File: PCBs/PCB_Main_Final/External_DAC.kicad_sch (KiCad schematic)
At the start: 15 parts, among them U9 PCM5102A

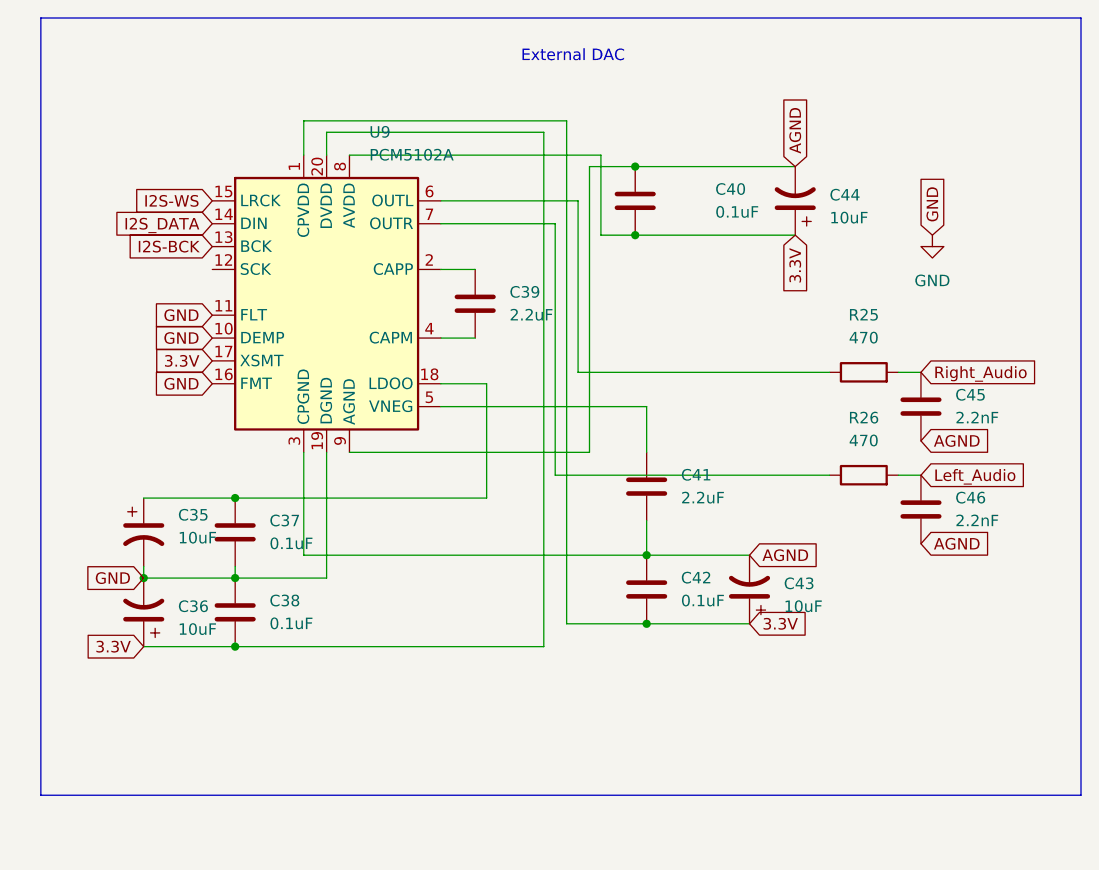
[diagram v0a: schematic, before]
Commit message: fixed vias and expanded boost converter
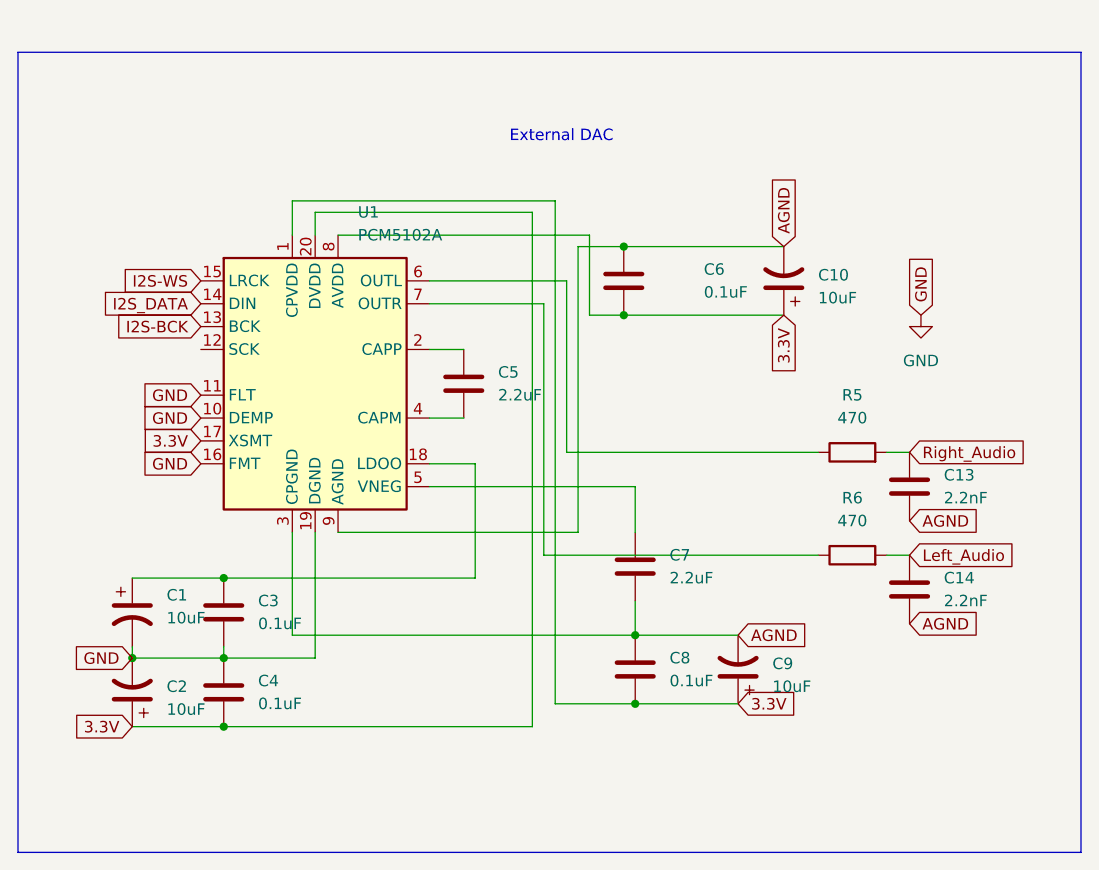
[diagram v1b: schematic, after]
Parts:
- removed C35, C36, C43, C44: 10uF, Artisyn_Components:EX_DAC_ELEC_CAPS_10uF, symbol Device:C_Polarized_US
- removed C37, C38, C40, C42: 0.1uF, Capacitor_SMD:C_0805_2012Metric, symbol Device:C
- removed C39, C41: 2.2uF, Capacitor_SMD:C_0805_2012Metric, symbol Device:C
- removed C45, C46: 2.2nF, Capacitor_SMD:C_0805_2012Metric, symbol Device:C
- removed R25, R26: 470, Resistor_SMD:R_0805_2012Metric, symbol Device:R
- removed U9: PCM5102A, Package_SO:TSSOP-20_4.4x6.5mm_P0.65mm, symbol Audio:PCM5102A
- added C1, C10, C2, C9: 10uF, Artisyn_Components:EX_DAC_ELEC_CAPS_10uF, symbol Device:C_Polarized_US
- added C13, C14: 2.2nF, Capacitor_SMD:C_0805_2012Metric, symbol Device:C
- added C3, C4, C6, C8: 0.1uF, Capacitor_SMD:C_0805_2012Metric, symbol Device:C
- added C5, C7: 2.2uF, Capacitor_SMD:C_0805_2012Metric, symbol Device:C
- added R5, R6: 470, Resistor_SMD:R_0805_2012Metric, symbol Device:R
- added U1: PCM5102A, Package_SO:TSSOP-20_4.4x6.5mm_P0.65mm, symbol Audio:PCM5102A
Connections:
- net 3.3V: now also C10.1, C2.1, C4.2, C6.2, C8.2, C9.1, U1.1 (CPVDD), U1.17 (XSMT), U1.20 (DVDD), U1.8 (AVDD)
- net AGND: now also C10.2, C13.2, C14.2, C6.1, C7.2, C8.1, C9.2, U1.3 (CPGND), U1.9 (AGND)
- net GND: now also C1.2, C2.2, C3.2, C4.1, U1.10 (DEMP), U1.11 (FLT), U1.16 (FMT), U1.19 (DGND)
- net I2S-BCK: now also U1.13 (BCK)
- net I2S-WS: now also U1.15 (LRCK)
- net I2S_DATA: now also U1.14 (DIN)
- net Left_Audio: now also C14.1, R6.2
- net Right_Audio: now also C13.1, R5.2
- new net: C7.1, U1.5 (VNEG)
- new net: R6.1, U1.7 (OUTR)
- new net: C5.1, U1.2 (CAPP)
- new net: C5.2, U1.4 (CAPM)
- new net: C1.1, C3.1, U1.18 (LDOO)
- new net: R5.1, U1.6 (OUTL)
